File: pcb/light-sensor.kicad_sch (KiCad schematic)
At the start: 3 parts

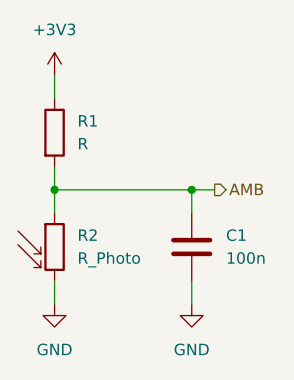
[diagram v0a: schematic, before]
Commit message: Remove sensor hub
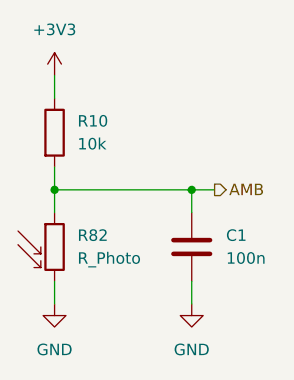
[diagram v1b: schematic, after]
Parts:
- C1: footprint (none) -> Capacitor_SMD:C_0402_1005Metric; LCSC (none) -> C1525
- R10: renamed from R1; value R -> 10k; footprint (none) -> Resistor_SMD:R_0402_1005Metric; LCSC (none) -> C25744
- R82: renamed from R2; footprint (none) -> Resistor_SMD:R_1210_3225Metric; LCSC (none) -> C2904880
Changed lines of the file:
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@@
 		(dnp no)
 		(fields_autoplaced yes)
-		(property "Reference" "#PWR063"
+		(property "Reference" "#PWR0102"
 			(at 60.96 82.55 0)
 			(effects
@@
 		(instances
 			(project "raven"
-				(path "/38b0a34b-2047-47f6-90d7-ccdf77e8e212/69f17c52-085e-4098-9317-47d7511472bd/e4ef8bfb-8ca4-4eda-88d6-8d711af4ddb5"
-					(reference "#PWR063")
-					(unit 1)
-				)
-				(path "/38b0a34b-2047-47f6-90d7-ccdf77e8e212/69f17c52-085e-4098-9317-47d7511472bd/ef67af30-d83a-493a-9361-758646c1cbba"
-					(reference "#PWR02")
+				(path "/38b0a34b-2047-47f6-90d7-ccdf77e8e212/11ab18bc-ce77-4033-8a5c-38e1164bac50"
+					(reference "#PWR0272")
+					(unit 1)
+				)
+				(path "/38b0a34b-2047-47f6-90d7-ccdf77e8e212/bf3906f2-c83b-4398-a50d-7d7e43f0335f"
+					(reference "#PWR0275")
 					(unit 1)
 				)
@@
 		(dnp no)
 		(fields_autoplaced yes)
-		(property "Reference" "R1"
+		(property "Reference" "R10"
 			(at 63.5 55.8799 0)
 			(effects
@@
 			)
 		)
-		(property "Value" "R"
+		(property "Value" "10k"
 			(at 63.5 58.4199 0)
 			(effects
@@
 			)
 		)
-		(property "Footprint" ""
+		(property "Footprint" "Resistor_SMD:R_0402_1005Metric"
 			(at 59.182 57.15 90)
 			(effects
@@
 			)
 		)
+		(property "LCSC" "C25744"
+			(at 60.96 57.15 0)
+			(effects
+				(font
+					(size 1.27 1.27)
+				)
+				(hide yes)
+			)
+		)
 		(pin "2"
 		)
@@
 		)
 		(instances
-			(project ""
-				(path "/38b0a34b-2047-47f6-90d7-ccdf77e8e212/69f17c52-085e-4098-9317-47d7511472bd/e4ef8bfb-8ca4-4eda-88d6-8d711af4ddb5"
-					(reference "R19")
-					(unit 1)
-				)
-				(path "/38b0a34b-2047-47f6-90d7-ccdf77e8e212/69f17c52-085e-4098-9317-47d7511472bd/ef67af30-d83a-493a-9361-758646c1cbba"
-					(reference "R1")
+			(project "raven"
+				(path "/38b0a34b-2047-47f6-90d7-ccdf77e8e212/11ab18bc-ce77-4033-8a5c-38e1164bac50"
+					(reference "R10")
+					(unit 1)
+				)
+				(path "/38b0a34b-2047-47f6-90d7-ccdf77e8e212/bf3906f2-c83b-4398-a50d-7d7e43f0335f"
+					(reference "R83")
 					(unit 1)
 				)
@@
 		(dnp no)
 		(fields_autoplaced yes)
-		(property "Reference" "#PWR01"
+		(property "Reference" "#PWR074"
 			(at 60.96 54.61 0)
 			(effects
@@
 		)
 		(instances
-			(project ""
-				(path "/38b0a34b-2047-47f6-90d7-ccdf77e8e212/69f17c52-085e-4098-9317-47d7511472bd/e4ef8bfb-8ca4-4eda-88d6-8d711af4ddb5"
-					(reference "#PWR062")
-					(unit 1)
-				)
-				(path "/38b0a34b-2047-47f6-90d7-ccdf77e8e212/69f17c52-085e-4098-9317-47d7511472bd/ef67af30-d83a-493a-9361-758646c1cbba"
-					(reference "#PWR01")
+			(project "raven"
+				(path "/38b0a34b-2047-47f6-90d7-ccdf77e8e212/11ab18bc-ce77-4033-8a5c-38e1164bac50"
+					(reference "#PWR074")
+					(unit 1)
+				)
+				(path "/38b0a34b-2047-47f6-90d7-ccdf77e8e212/bf3906f2-c83b-4398-a50d-7d7e43f0335f"
+					(reference "#PWR0274")
 					(unit 1)
 				)
@@
 		(dnp no)
 		(fields_autoplaced yes)
-		(property "Reference" "#PWR064"
+		(property "Reference" "#PWR0103"
 			(at 76.2 82.55 0)
 			(effects
@@
 		(instances
 			(project "raven"
-				(path "/38b0a34b-2047-47f6-90d7-ccdf77e8e212/69f17c52-085e-4098-9317-47d7511472bd/e4ef8bfb-8ca4-4eda-88d6-8d711af4ddb5"
-					(reference "#PWR064")
-					(unit 1)
-				)
-				(path "/38b0a34b-2047-47f6-90d7-ccdf77e8e212/69f17c52-085e-4098-9317-47d7511472bd/ef67af30-d83a-493a-9361-758646c1cbba"
-					(reference "#PWR03")
+				(path "/38b0a34b-2047-47f6-90d7-ccdf77e8e212/11ab18bc-ce77-4033-8a5c-38e1164bac50"
+					(reference "#PWR0273")
+					(unit 1)
+				)
+				(path "/38b0a34b-2047-47f6-90d7-ccdf77e8e212/bf3906f2-c83b-4398-a50d-7d7e43f0335f"
+					(reference "#PWR0276")
 					(unit 1)
 				)
@@
 			)
 		)
-		(property "Footprint" ""
+		(property "Footprint" "Capacitor_SMD:C_0402_1005Metric"
 			(at 77.1652 73.66 0)
 			(effects
@@
 			)
 		)
+		(property "LCSC" "C1525"
+			(at 76.2 69.85 0)
+			(effects
+				(font
+					(size 1.27 1.27)
+				)
+				(hide yes)
+			)
+		)
+		(pin "1"
+		)
 		(pin "2"
 		)
-		(pin "1"
-		)
-		(instances
-			(project ""
-				(path "/38b0a34b-2047-47f6-90d7-ccdf77e8e212/69f17c52-085e-4098-9317-47d7511472bd/e4ef8bfb-8ca4-4eda-88d6-8d711af4ddb5"
-					(reference "C12")
-					(unit 1)
-				)
-				(path "/38b0a34b-2047-47f6-90d7-ccdf77e8e212/69f17c52-085e-4098-9317-47d7511472bd/ef67af30-d83a-493a-9361-758646c1cbba"
-					(reference "C1")
+		(instances
+			(project "raven"
+				(path "/38b0a34b-2047-47f6-90d7-ccdf77e8e212/11ab18bc-ce77-4033-8a5c-38e1164bac50"
+					(reference "C21")
+					(unit 1)
+				)
+				(path "/38b0a34b-2047-47f6-90d7-ccdf77e8e212/bf3906f2-c83b-4398-a50d-7d7e43f0335f"
+					(reference "C22")
 					(unit 1)
 				)
@@
 		(dnp no)
 		(fields_autoplaced yes)
-		(property "Reference" "R2"
+		(property "Reference" "R82"
 			(at 63.5 68.5799 0)
 			(effects
@@
 			)
 		)
-		(property "Footprint" ""
+		(property "Footprint" "Resistor_SMD:R_1210_3225Metric"
 			(at 62.23 76.2 90)
 			(effects
@@
 			)
 		)
+		(property "LCSC" "C2904880"
+			(at 60.96 69.85 0)
+			(effects
+				(font
+					(size 1.27 1.27)
+				)
+				(hide yes)
+			)
+		)
 		(pin "1"
 		)
@@
 		)
 		(instances
-			(project ""
-				(path "/38b0a34b-2047-47f6-90d7-ccdf77e8e212/69f17c52-085e-4098-9317-47d7511472bd/e4ef8bfb-8ca4-4eda-88d6-8d711af4ddb5"
-					(reference "R20")
-					(unit 1)
-				)
-				(path "/38b0a34b-2047-47f6-90d7-ccdf77e8e212/69f17c52-085e-4098-9317-47d7511472bd/ef67af30-d83a-493a-9361-758646c1cbba"
-					(reference "R2")
-					(unit 1)
-				)
+			(project "raven"
+				(path "/38b0a34b-2047-47f6-90d7-ccdf77e8e212/11ab18bc-ce77-4033-8a5c-38e1164bac50"
+					(reference "R82")
+					(unit 1)
+				)
+				(path "/38b0a34b-2047-47f6-90d7-ccdf77e8e212/bf3906f2-c83b-4398-a50d-7d7e43f0335f"
+					(reference "R84")
+					(unit 1)
+				)

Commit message: Finish schematic
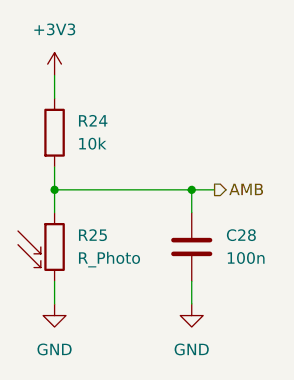
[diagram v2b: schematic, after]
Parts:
- renumbered C1 to C28, R10 to R24, R82 to R25
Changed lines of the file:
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@@
 		(dnp no)
 		(fields_autoplaced yes)
-		(property "Reference" "#PWR0102"
+		(property "Reference" "#PWR078"
 			(at 60.96 82.55 0)
 			(effects
@@
 		(instances
 			(project "raven"
-				(path "/38b0a34b-2047-47f6-90d7-ccdf77e8e212/11ab18bc-ce77-4033-8a5c-38e1164bac50"
-					(reference "#PWR0272")
-					(unit 1)
-				)
-				(path "/38b0a34b-2047-47f6-90d7-ccdf77e8e212/bf3906f2-c83b-4398-a50d-7d7e43f0335f"
-					(reference "#PWR0275")
+				(path "/38b0a34b-2047-47f6-90d7-ccdf77e8e212/7e3f67f4-c7a7-4f15-a62c-4903c0d88b19/f227bbf4-2b20-4d75-886f-a4b89b58a946"
+					(reference "#PWR078")
 					(unit 1)
 				)
@@
 		(dnp no)
 		(fields_autoplaced yes)
-		(property "Reference" "R10"
+		(property "Reference" "R24"
 			(at 63.5 55.8799 0)
 			(effects
@@
 		(instances
 			(project "raven"
-				(path "/38b0a34b-2047-47f6-90d7-ccdf77e8e212/11ab18bc-ce77-4033-8a5c-38e1164bac50"
-					(reference "R10")
-					(unit 1)
-				)
-				(path "/38b0a34b-2047-47f6-90d7-ccdf77e8e212/bf3906f2-c83b-4398-a50d-7d7e43f0335f"
-					(reference "R83")
+				(path "/38b0a34b-2047-47f6-90d7-ccdf77e8e212/7e3f67f4-c7a7-4f15-a62c-4903c0d88b19/f227bbf4-2b20-4d75-886f-a4b89b58a946"
+					(reference "R24")
 					(unit 1)
 				)
@@
 		(dnp no)
 		(fields_autoplaced yes)
-		(property "Reference" "#PWR074"
+		(property "Reference" "#PWR077"
 			(at 60.96 54.61 0)
 			(effects
@@
 		(instances
 			(project "raven"
-				(path "/38b0a34b-2047-47f6-90d7-ccdf77e8e212/11ab18bc-ce77-4033-8a5c-38e1164bac50"
-					(reference "#PWR074")
-					(unit 1)
-				)
-				(path "/38b0a34b-2047-47f6-90d7-ccdf77e8e212/bf3906f2-c83b-4398-a50d-7d7e43f0335f"
-					(reference "#PWR0274")
+				(path "/38b0a34b-2047-47f6-90d7-ccdf77e8e212/7e3f67f4-c7a7-4f15-a62c-4903c0d88b19/f227bbf4-2b20-4d75-886f-a4b89b58a946"
+					(reference "#PWR077")
 					(unit 1)
 				)
@@
 		(dnp no)
 		(fields_autoplaced yes)
-		(property "Reference" "#PWR0103"
+		(property "Reference" "#PWR079"
 			(at 76.2 82.55 0)
 			(effects
@@
 		(instances
 			(project "raven"
-				(path "/38b0a34b-2047-47f6-90d7-ccdf77e8e212/11ab18bc-ce77-4033-8a5c-38e1164bac50"
-					(reference "#PWR0273")
-					(unit 1)
-				)
-				(path "/38b0a34b-2047-47f6-90d7-ccdf77e8e212/bf3906f2-c83b-4398-a50d-7d7e43f0335f"
-					(reference "#PWR0276")
+				(path "/38b0a34b-2047-47f6-90d7-ccdf77e8e212/7e3f67f4-c7a7-4f15-a62c-4903c0d88b19/f227bbf4-2b20-4d75-886f-a4b89b58a946"
+					(reference "#PWR079")
 					(unit 1)
 				)
@@
 		(dnp no)
 		(fields_autoplaced yes)
-		(property "Reference" "C1"
+		(property "Reference" "C28"
 			(at 80.01 68.5799 0)
 			(effects
@@
 		(instances
 			(project "raven"
-				(path "/38b0a34b-2047-47f6-90d7-ccdf77e8e212/11ab18bc-ce77-4033-8a5c-38e1164bac50"
-					(reference "C21")
-					(unit 1)
-				)
-				(path "/38b0a34b-2047-47f6-90d7-ccdf77e8e212/bf3906f2-c83b-4398-a50d-7d7e43f0335f"
-					(reference "C22")
+				(path "/38b0a34b-2047-47f6-90d7-ccdf77e8e212/7e3f67f4-c7a7-4f15-a62c-4903c0d88b19/f227bbf4-2b20-4d75-886f-a4b89b58a946"
+					(reference "C28")
 					(unit 1)
 				)
@@
 		(dnp no)
 		(fields_autoplaced yes)
-		(property "Reference" "R82"
+		(property "Reference" "R25"
 			(at 63.5 68.5799 0)
 			(effects
@@
 		(instances
 			(project "raven"
-				(path "/38b0a34b-2047-47f6-90d7-ccdf77e8e212/11ab18bc-ce77-4033-8a5c-38e1164bac50"
-					(reference "R82")
-					(unit 1)
-				)
-				(path "/38b0a34b-2047-47f6-90d7-ccdf77e8e212/bf3906f2-c83b-4398-a50d-7d7e43f0335f"
-					(reference "R84")
-					(unit 1)
-				)
+				(path "/38b0a34b-2047-47f6-90d7-ccdf77e8e212/7e3f67f4-c7a7-4f15-a62c-4903c0d88b19/f227bbf4-2b20-4d75-886f-a4b89b58a946"
+					(reference "R25")
+					(unit 1)
+				)
